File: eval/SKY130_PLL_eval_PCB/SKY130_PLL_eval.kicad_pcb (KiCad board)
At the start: 4 copper layers, 60.1 x 84 mm, 55 parts, among them J3 Conn_02x07_Odd_Even, J5 Conn_02x07_Odd_Even, J6 Conn_02x06_Odd_Even, J7 Conn_02x13_Odd_Even, U1 ADM7154ARDZ-1.8-R7, U2 Caravel_QFN, U3 AD8000YCPZ-REEL7

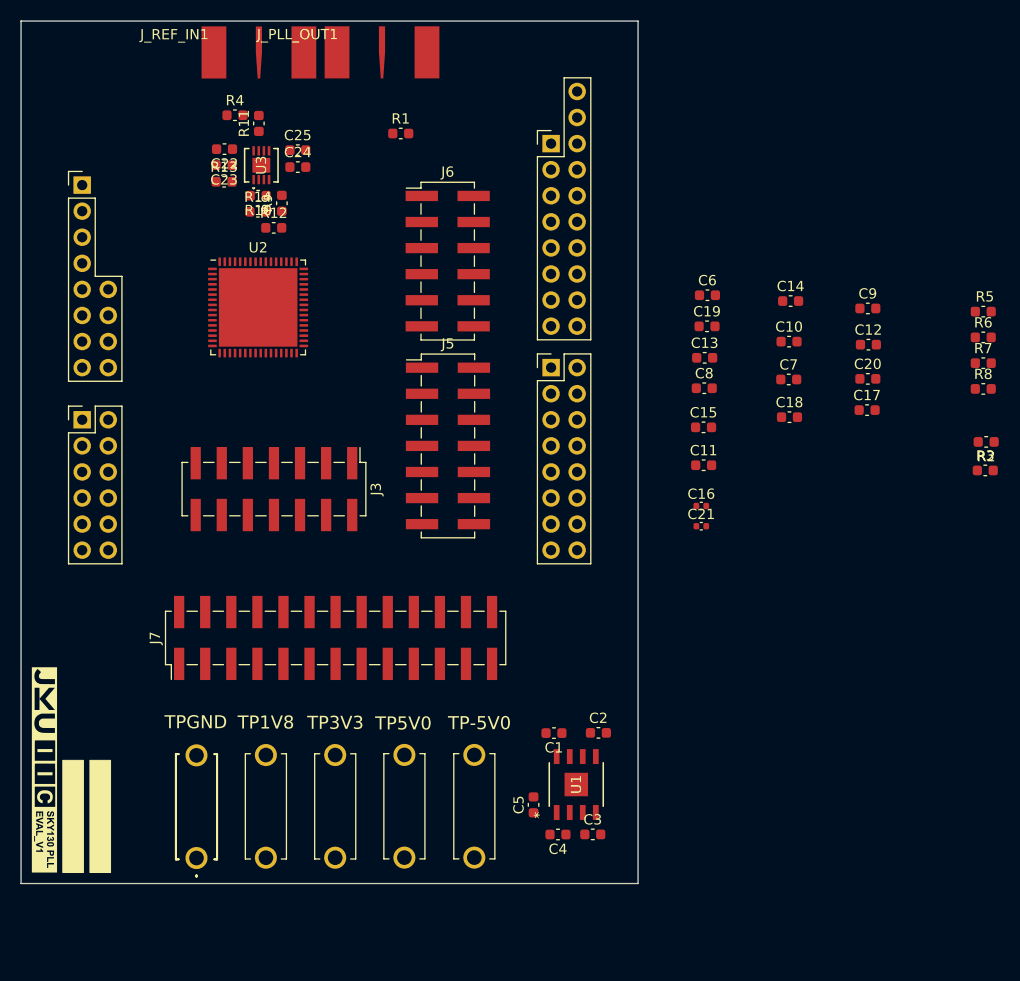
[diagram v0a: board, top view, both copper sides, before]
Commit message: eval pcb added
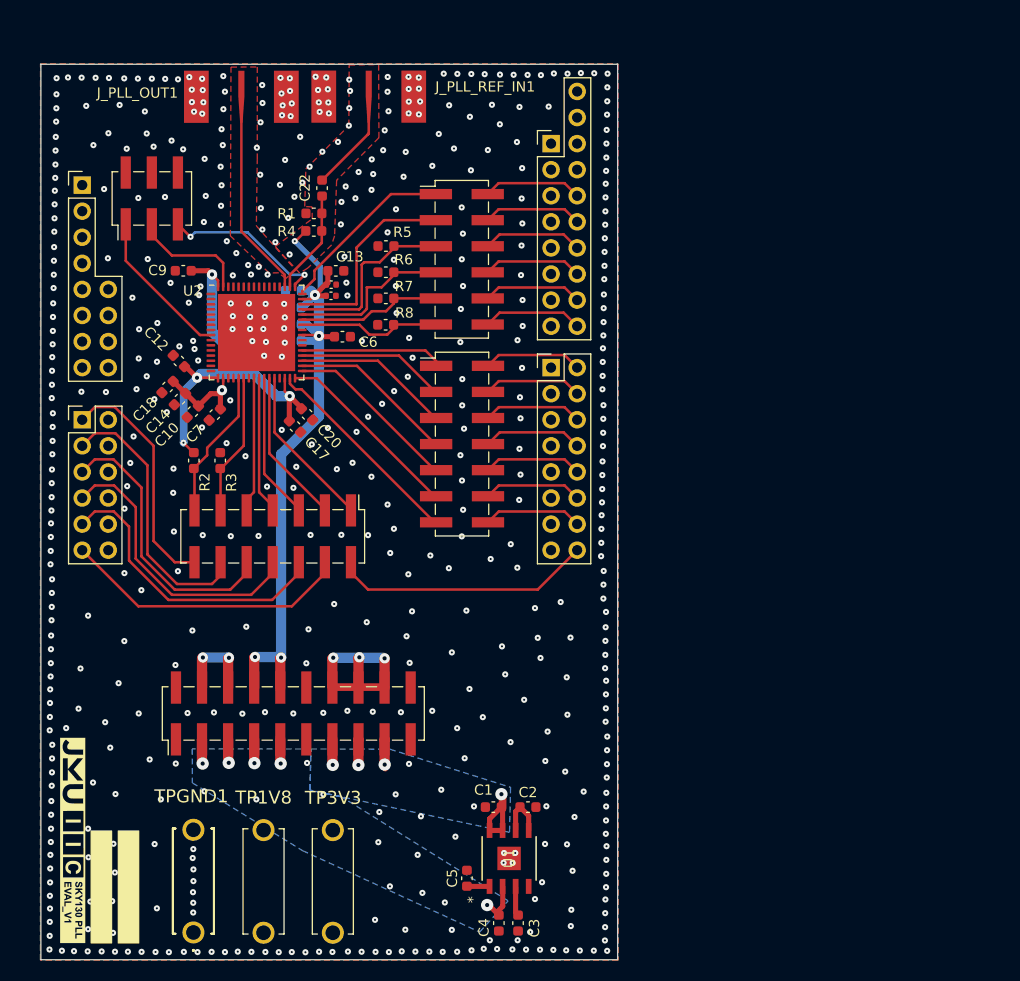
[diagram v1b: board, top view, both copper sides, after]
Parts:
- removed C23, C25: 100n, Capacitor_SMD:C_0603_1608Metric
- removed C24: 10u, Capacitor_SMD:C_0603_1608Metric
- removed J7: Conn_02x13_Odd_Even, Connector_PinHeader_2.54mm:PinHeader_2x13_P2.54mm_Vertical_SMD
- removed J_REF_IN1: 142-0701-851_TO_SENSO1, TO_SENSO1:142-0701-851_TO_SENSO1
- removed R10, R14: 432, Capacitor_SMD:C_0603_1608Metric
- removed R11, R9: 50, Capacitor_SMD:C_0603_1608Metric
- removed R12: DNP, Capacitor_SMD:C_0603_1608Metric
- removed R13: 0, Capacitor_SMD:C_0603_1608Metric
- removed TP-5V0, TP5V0: Mini_Banana_Plug_Red, TO_SENSO1:930224101
- removed TPGND: Mini_Banana_Plug_Black, TO_SENSO1:930224100
- removed U3: AD8000YCPZ-REEL7, ad8000ycpz:CP_8_13_ADI
- added J1: Conn_02x10_Odd_Even, Connector_PinHeader_2.54mm:PinHeader_2x10_P2.54mm_Vertical_SMD, F.Cu at (125.9, 131.6)
- added J2: Conn_02x03_Odd_Even, Connector_PinHeader_2.54mm:PinHeader_2x03_P2.54mm_Vertical_SMD, F.Cu at (112.1, 81.4)
- added J_PLL_REF_IN1: 142-0701-851_TO_SENSO1, TO_SENSO1:142-0701-851_TO_SENSO1, F.Cu at (133.2, 71.3)
- added TPGND1: Mini_Banana_Plug_Black, TO_SENSO1:930224100, F.Cu at (116.2, 152.9)
- C11, C15, C19, C8: moved to B.Cu
- C22: value 10u -> 1n
- R1: value 50 -> 100
- R4: value DNP -> 100
- moved R2 77.2 mm to (116.2, 106.9), turned to -90 degrees
- moved R3 74.5 mm to (118.8, 106.9), turned to 90 degrees
- moved C12 67.2 mm to (114.7, 97.2), turned to 135 degrees
- moved C9 66.8 mm to (115.2, 88.5), turned to 180 degrees
- moved C18 60.7 mm to (113.6, 99.8), turned to -135 degrees
- moved C14 60.2 mm to (114.8, 101.0), turned to -135 degrees
- moved R8 58.5 mm to (134.9, 93.7), turned to 180 degrees
- moved R6 58.5 mm to (134.9, 88.6), turned to 180 degrees
- moved R7 58.5 mm to (134.9, 91.2), turned to 180 degrees
- moved R5 58.5 mm to (134.9, 86.0), turned to 180 degrees
- moved C10 58.5 mm to (116.1, 102.2), turned to -135 degrees
- moved C7 56.0 mm to (118.2, 102.5), turned to -135 degrees
- moved C17 55.8 mm to (126.0, 103.6), turned to -45 degrees
- moved C20 54.7 mm to (127.2, 102.5), turned to -45 degrees
- moved C21 43.0 mm to (129.6, 89.8)
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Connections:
- C22 pad 1: VDD_5V0_AMP -> /PLL_IO/pll_sma_in
- C22 pad 2: GND -> pll_ref_in
- J_PLL_OUT1 pad 1: pll_ref_in -> pll_out
- R4 pad 1: /PLL_IO/pll_out_misc -> VDD_1V8_PLL
- R4 pad 2: /PLL_IO/pll_out_50Ohm -> pll_ref_in
- U2 pad 49: unconnected-(U2-vccd1-Pad49) -> /IC_Packaged/vccd1
- U2 pad 63: unconnected-(U2-vccd2-Pad63) -> /IC_Packaged/vccd2
- U2 pad 9: unconnected-(U2-vdda2-Pad9) -> /IC_Packaged/vdda2
- XA1 pad A2: gpio_arty -> flash_csb_arty
- XA1 pad A3: flash_csb_arty -> flash_clk_arty
- XA1 pad A4: flash_clk_arty -> flash_io2_arty
- XA1 pad A5: flash_io2_arty -> flash_io1_arty
- XA1 pad IO0: flash_io1_arty -> gpio_arty
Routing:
- net VDD_1V8_PLL: track 0.00 -> 70.0 mm, vias 0 -> 5
- net VDD_3V3: track 0.00 -> 62.3 mm, vias 0 -> 7
- net flash_io2_arty: track 0.00 -> 29.3 mm
- net flash_clk_arty: track 0.00 -> 28.4 mm
- net flash_io1_arty: track 0.00 -> 28.3 mm
- net flash_csb_arty: track 0.00 -> 27.5 mm
- net mgmt_clk_arty: track 0.00 -> 26.8 mm
- net gpio_arty: track 0.00 -> 25.3 mm
- net mgmt_rstb_arty: track 0.00 -> 23.1 mm
- net /IC_Packaged/ser_jtag: track 0.00 -> 20.4 mm
- net /IC_Packaged/pll_sin: track 0.00 -> 19.6 mm
- net pll_out: track 0.00 -> 19.0 mm
- net /IC_Packaged/ser_sdo: track 0.00 -> 18.5 mm
- net VDD_1V8_MGMT: track 0.00 -> 18.4 mm, vias 0 -> 3
- net /IC_Packaged/pll_load: track 0.00 -> 18.1 mm
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- added copper zone on In2.Cu, net /Power/VDD_1V8_EXT
- added copper zone on B.Cu, net /Power/VDD_1V8_LDO
- added copper zone on In2.Cu, net /Power/VDD_3V3_EXT
- added copper zone on B.Cu, net /Power/VDD_3V3_LDO
- added copper zone on B.Cu, net GND
- added copper zone on F.Cu, net GND
- added copper zone on In1.Cu, net GND
- added copper zone on In2.Cu, net VDD_1V8_MGMT
- added copper zone on In2.Cu, net VDD_1V8_PLL
- added copper zone on In2.Cu, net VDD_3V3
- added copper zone on In2.Cu, net VDD_3V3_ARTY
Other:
- board size 60.1 x 84 mm -> 56.2 x 87.2 mm

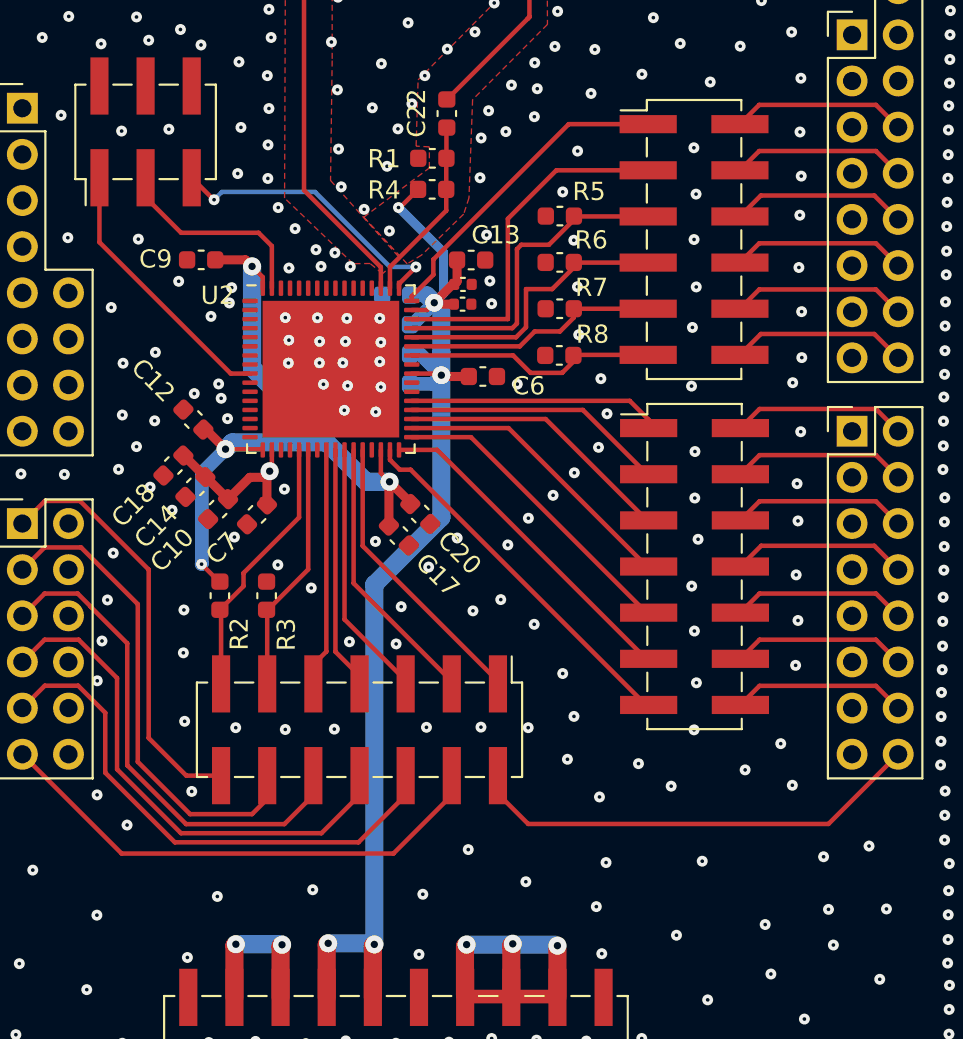
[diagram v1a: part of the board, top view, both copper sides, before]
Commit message: pin header labeling inserted
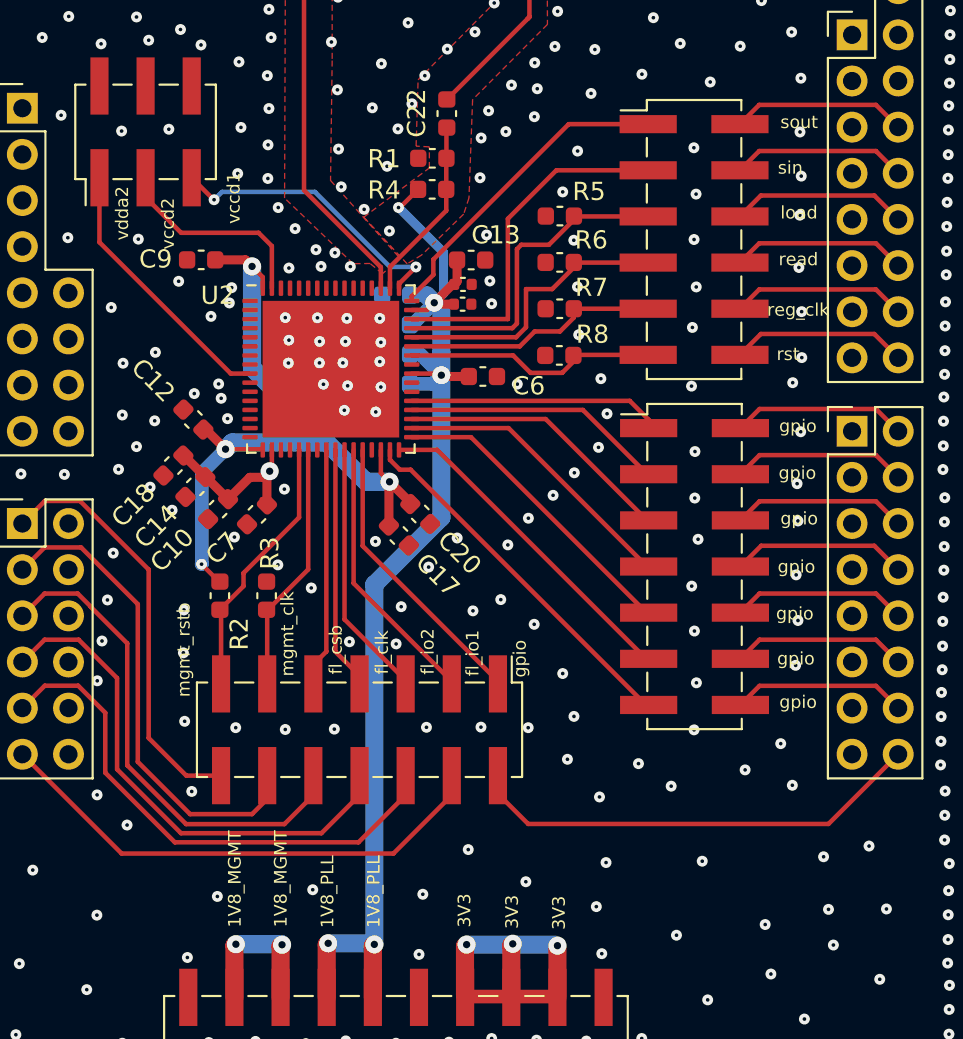
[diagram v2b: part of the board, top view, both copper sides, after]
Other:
- board text added: "1V8_MGMT"
- board text added: "1V8_PLL"
- board text added: "3V3"
- board text added: "fl_clk"
- board text added: "fl_csb"
- board text added: "fl_io1"
- board text added: "fl_io2"
- board text added: "gpio"
- board text added: "load"
- board text added: "mgmt_clk"
- board text added: "mgmt_rstb"
- board text added: "read"
- board text added: "reg_clk"
- board text added: "rst"
- board text added: "sin"
- board text added: "sout"
- board text added: "vccd1"
- board text added: "vccd2"
- board text added: "vdda2"
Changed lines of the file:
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@@
     (property "ki_keywords" "R res resistor")
     (attr smd)
-    (fp_text reference "R3" (at -2.135 1.09 90) (layer "F.SilkS")
+    (fp_text reference "R3" (at 2.345 0.18 90) (layer "F.SilkS")
         (effects (font (size 1 1) (thickness 0.15)))
     )
@@
   (gr_rect (start 101.29 68.345) (end 157.47 155.565)
     (stroke (width 0.1) (type default)) (fill none) (layer "Edge.Cuts"))
+  (gr_text "3V3" (at 135.26 125.34 90) (layer "F.SilkS")
+    (effects (font (size 0.7 0.7) (thickness 0.125)) (justify left bottom))
+  )
+  (gr_text "vccd2" (at 113.74 87.89 90) (layer "F.SilkS")
+    (effects (font (size 0.7 0.7) (thickness 0.125)) (justify left bottom))
+  )
+  (gr_text "mgmt_clk" (at 120.32 111.39 90) (layer "F.SilkS")
+    (effects (font (size 0.7 0.7) (thickness 0.125)) (justify left bottom))
+  )
+  (gr_text "gpio" (at 146.86 110.82) (layer "F.SilkS")
+    (effects (font (size 0.7 0.7) (thickness 0.125)) (justify left bottom))
+  )
+  (gr_text "3V3" (at 132.68 125.29 90) (layer "F.SilkS")
+    (effects (font (size 0.7 0.7) (thickness 0.125)) (justify left bottom))
+  )
+  (gr_text "gpio" (at 146.98 113.21) (layer "F.SilkS")
+    (effects (font (size 0.7 0.7) (thickness 0.125)) (justify left bottom))
+  )
+  (gr_text "1V8_MGMT" (at 119.95 125.2 90) (layer "F.SilkS")
+    (effects (font (size 0.7 0.7) (thickness 0.125)) (justify left bottom))
+  )
+  (gr_text "reg_clk" (at 146.31 91.62) (layer "F.SilkS")
+    (effects (font (size 0.7 0.7) (thickness 0.125)) (justify left bottom))
+  )
+  (gr_text "mgmt_rstb" (at 114.61 112.53 90) (layer "F.SilkS")
+    (effects (font (size 0.7 0.7) (thickness 0.125)) (justify left bottom))
+  )
+  (gr_text "fl_io1" (at 130.51 111.38 90) (layer "F.SilkS")
+    (effects (font (size 0.7 0.7) (thickness 0.125)) (justify left bottom))
+  )
+  (gr_text "gpio" (at 146.89 105.76) (layer "F.SilkS")
+    (effects (font (size 0.7 0.7) (thickness 0.125)) (justify left bottom))
+  )
+  (gr_text "gpio" (at 146.94 100.6) (layer "F.SilkS")
+    (effects (font (size 0.7 0.7) (thickness 0.125)) (justify left bottom))
+  )
+  (gr_text "gpio" (at 147.04 103.11) (layer "F.SilkS")
+    (effects (font (size 0.7 0.7) (thickness 0.125)) (justify left bottom))
+  )
+  (gr_text "rst" (at 146.83 94.06) (layer "F.SilkS")
+    (effects (font (size 0.7 0.7) (thickness 0.125)) (justify left bottom))
+  )
+  (gr_text "vccd1" (at 117.36 86.48 90) (layer "F.SilkS")
+    (effects (font (size 0.7 0.7) (thickness 0.125)) (justify left bottom))
+  )
+  (gr_text "load" (at 147.04 86.27) (layer "F.SilkS")
+    (effects (font (size 0.7 0.7) (thickness 0.125)) (justify left bottom))
+  )
+  (gr_text "gpio" (at 146.8 108.34) (layer "F.SilkS")
+    (effects (font (size 0.7 0.7) (thickness 0.125)) (justify left bottom))
+  )
+  (gr_text "sout" (at 147.04 81.29) (layer "F.SilkS")
+    (effects (font (size 0.7 0.7) (thickness 0.125)) (justify left bottom))
+  )
+  (gr_text "gpio" (at 146.97 98.02) (layer "F.SilkS")
+    (effects (font (size 0.7 0.7) (thickness 0.125)) (justify left bottom))
+  )
+  (gr_text "1V8_PLL" (at 122.52 125.24 90) (layer "F.SilkS")
+    (effects (font (size 0.7 0.7) (thickness 0.125)) (justify left bottom))
+  )
+  (gr_text "fl_clk" (at 125.52 111.28 90) (layer "F.SilkS")
+    (effects (font (size 0.7 0.7) (thickness 0.125)) (justify left bottom))
+  )
+  (gr_text "1V8_PLL" (at 125.06 125.23 90) (layer "F.SilkS")
+    (effects (font (size 0.7 0.7) (thickness 0.125)) (justify left bottom))
+  )
+  (gr_text "3V3" (at 130.06 125.21 90) (layer "F.SilkS")
+    (effects (font (size 0.7 0.7) (thickness 0.125)) (justify left bottom))
+  )
+  (gr_text "fl_io2" (at 128.04 111.29 90) (layer "F.SilkS")
+    (effects (font (size 0.7 0.7) (thickness 0.125)) (justify left bottom))
+  )
+  (gr_text "1V8_MGMT" (at 117.42 125.21 90) (layer "F.SilkS")
+    (effects (font (size 0.7 0.7) (thickness 0.125)) (justify left bottom))
+  )
+  (gr_text "sin" (at 146.9 83.8) (layer "F.SilkS")
+    (effects (font (size 0.7 0.7) (thickness 0.125)) (justify left bottom))
+  )
+  (gr_text "read" (at 146.94 88.84) (layer "F.SilkS")
+    (effects (font (size 0.7 0.7) (thickness 0.125)) (justify left bottom))
+  )
+  (gr_text "gpio" (at 133.11 111.45 90) (layer "F.SilkS")
+    (effects (font (size 0.7 0.7) (thickness 0.125)) (justify left bottom))
+  )
+  (gr_text "vdda2" (at 111.22 87.39 90) (layer "F.SilkS")
+    (effects (font (size 0.7 0.7) (thickness 0.125)) (justify left bottom))
+  )
+  (gr_text "fl_csb" (at 122.98 111.28 90) (layer "F.SilkS")
+    (effects (font (size 0.7 0.7) (thickness 0.125)) (justify left bottom))
+  )
   (segment (start 144.995 142.97585) (end 146.265 142.97585) (width 0.5) (layer "F.Cu") (net 1))
   (segment (start 146.265 142.97585) (end 146.265 140.825) (width 0.5) (layer "F.Cu") (net 1))

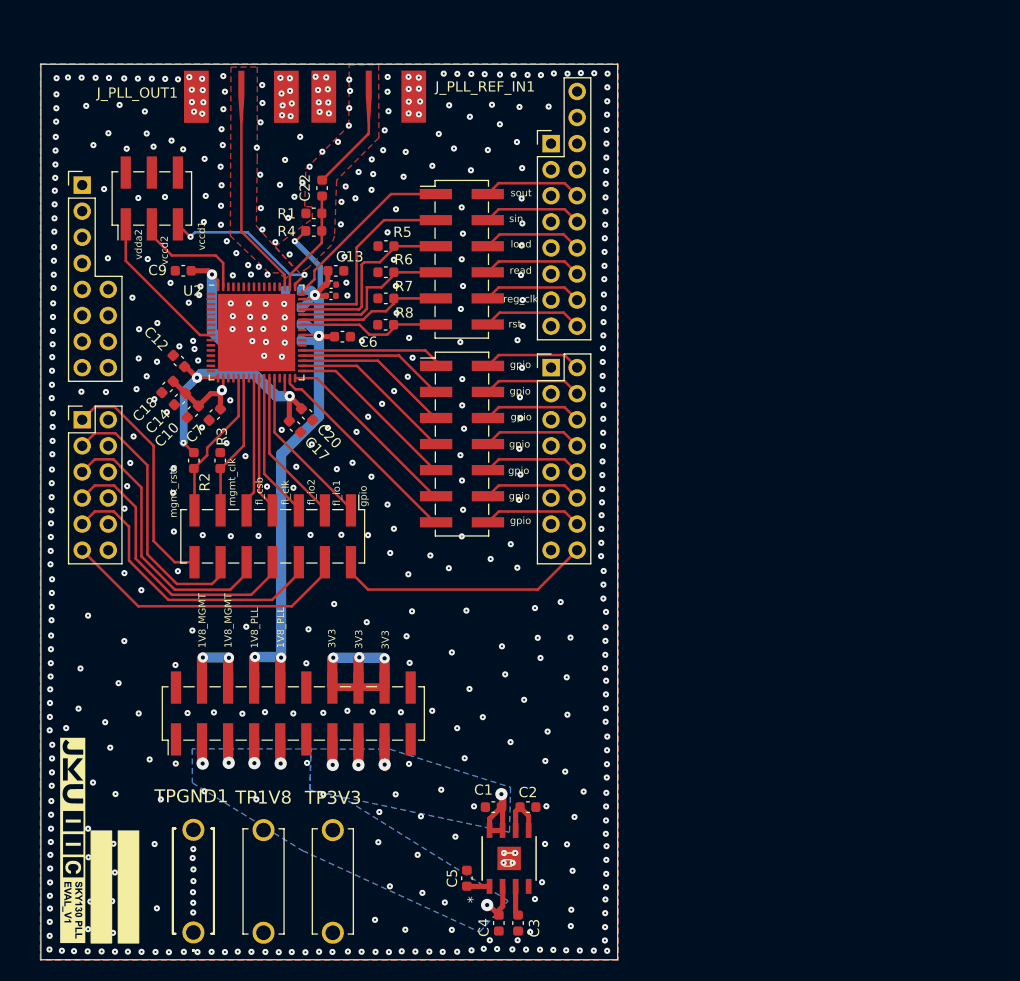
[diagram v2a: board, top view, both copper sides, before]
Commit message: labels updated
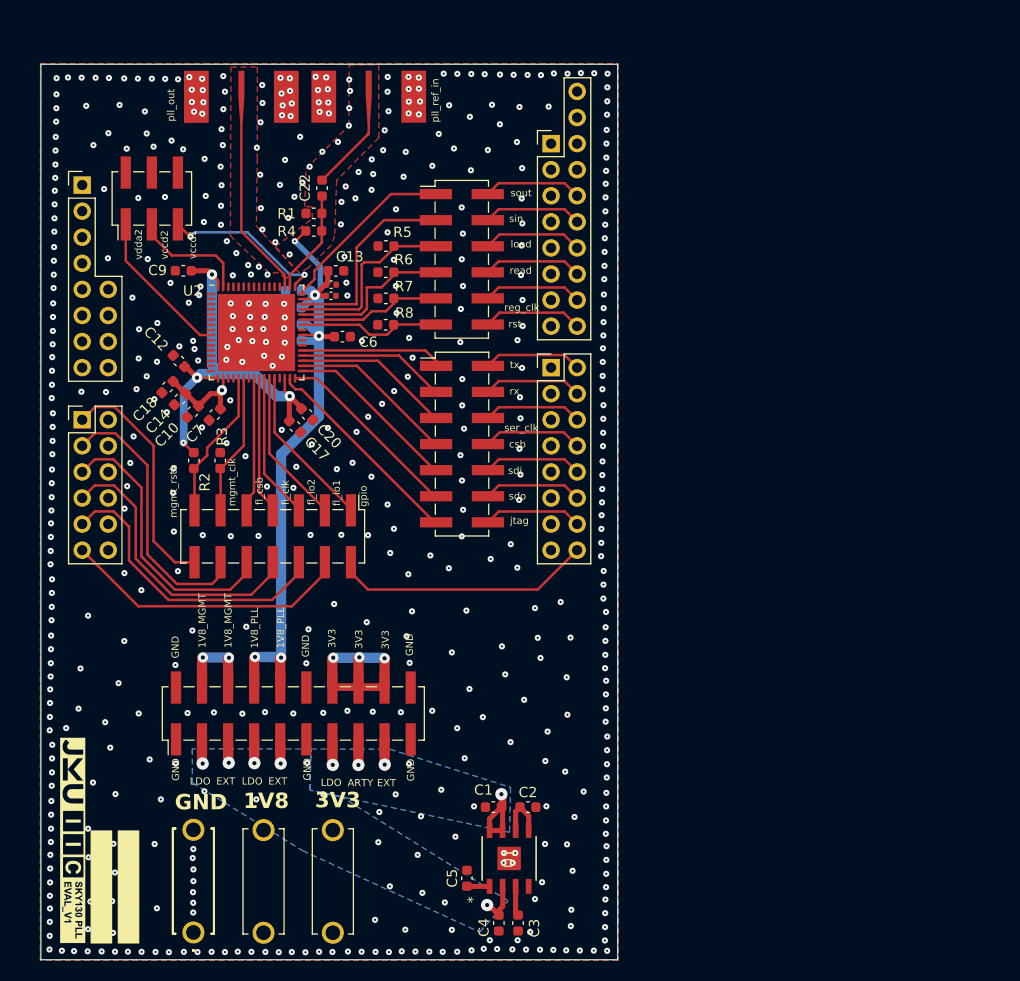
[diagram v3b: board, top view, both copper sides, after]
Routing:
- net VDD_3V3: track 62.3 -> 64.2 mm
- net GND: vias 529 -> 534
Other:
- board text added: "1V8"
- board text added: "ARTY"
- board text added: "EXT"
- board text added: "GND"
- board text added: "LDO"
- board text added: "csb"
- board text added: "jtag"
- board text added: "pll_out"
- board text added: "pll_ref_in"
- board text added: "rx"
- board text added: "sdi"
- board text added: "sdo"
- board text added: "ser_clk"
- board text added: "tx"
